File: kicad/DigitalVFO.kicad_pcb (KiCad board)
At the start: 2 copper layers, 99.6 x 49.8 mm, 34 parts, among them Q1 2N2222A, U1 74HC14, U2 Teensy3.2, U3 LCD1602A, U4 DDS-60

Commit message: Version 1.4
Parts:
- removed Battery: Battery, DigitalVFO:Conn_Power_2
- removed RF out: RF Out, DigitalVFO:BNC_Socket
- removed Rotary Encoder: Rotary_Encoder_Switch, DigitalVFO:Conn_RE_Switch
- removed SW_LED: SW_LED, DigitalVFO:Conn_Power_2
- added C8: 0.1uF, DigitalVFO:Cap_SmV, F.Cu at (182.9, 115.6)
- added J1: RF Out, DigitalVFO:BNC_Socket_TYCO-AMP, F.Cu at (214.6, 113.3)
- added J2: Battery, DigitalVFO:Conn_Power_2, F.Cu at (149.1, 112.3)
- added J3: SW_LED, DigitalVFO:Conn_Power_2, F.Cu at (174.8, 112.3)
- added R12: 39K, DigitalVFO:Res_SmH, F.Cu at (185.4, 109.7)
- added R13: 10K, DigitalVFO:Res_SmH, F.Cu at (185.4, 112.8)
- added SW1: Rotary_Encoder, DigitalVFO:Conn_RE_Switch, F.Cu at (161.8, 112.3)
- moved REF** 11.0 mm to (198.9, 112.5)
- moved R9 3.30 mm to (183.9, 102.4)
- moved R10 3.21 mm to (180.8, 102.6)
- moved C4 2.50 mm to (187.5, 102.4)
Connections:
- U2 pad 21: (no net) -> Net-(C8-Pad1)
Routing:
- net Net-(C8-Pad1): track 0.00 -> 32.3 mm
- net Net-(D1-Pad2): track 7.95 -> 38.4 mm
- net Net-(J1-Pad1): track 90.8 -> 86.3 mm
- net Net-(R9-Pad2): track 34.5 -> 30.7 mm
- net Net-(C4-Pad1): track 46.6 -> 44.1 mm
- net Net-(C2-Pad1): track 14.0 -> 14.7 mm
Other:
- net class Default: trace_width 0.25 -> 0.5
- board text added: "DigitalVFO 1.4 27 Apr 2018 vk4fawr"
- board text removed: "DigitalVFO 1.2 26 Mar 2018 vk4fawr"

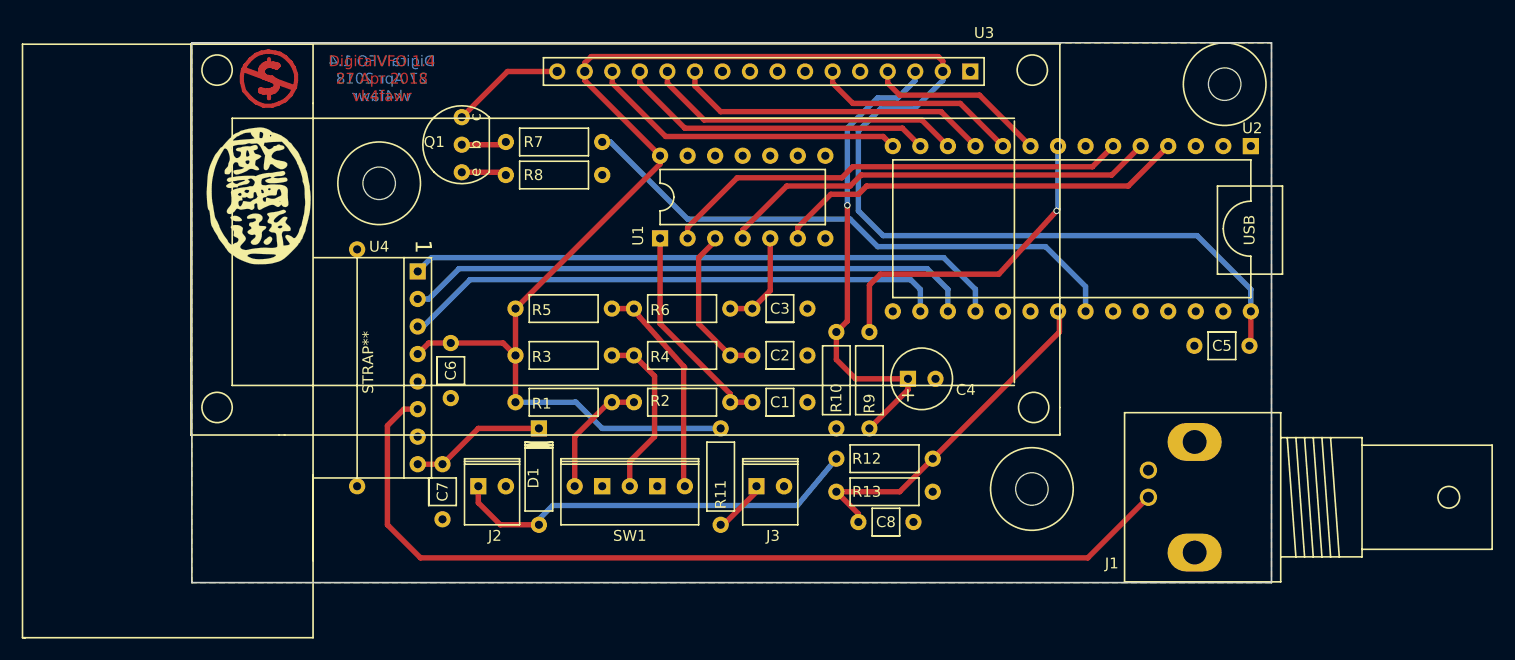
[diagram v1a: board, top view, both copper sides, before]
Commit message: v1.5 - more compact layout
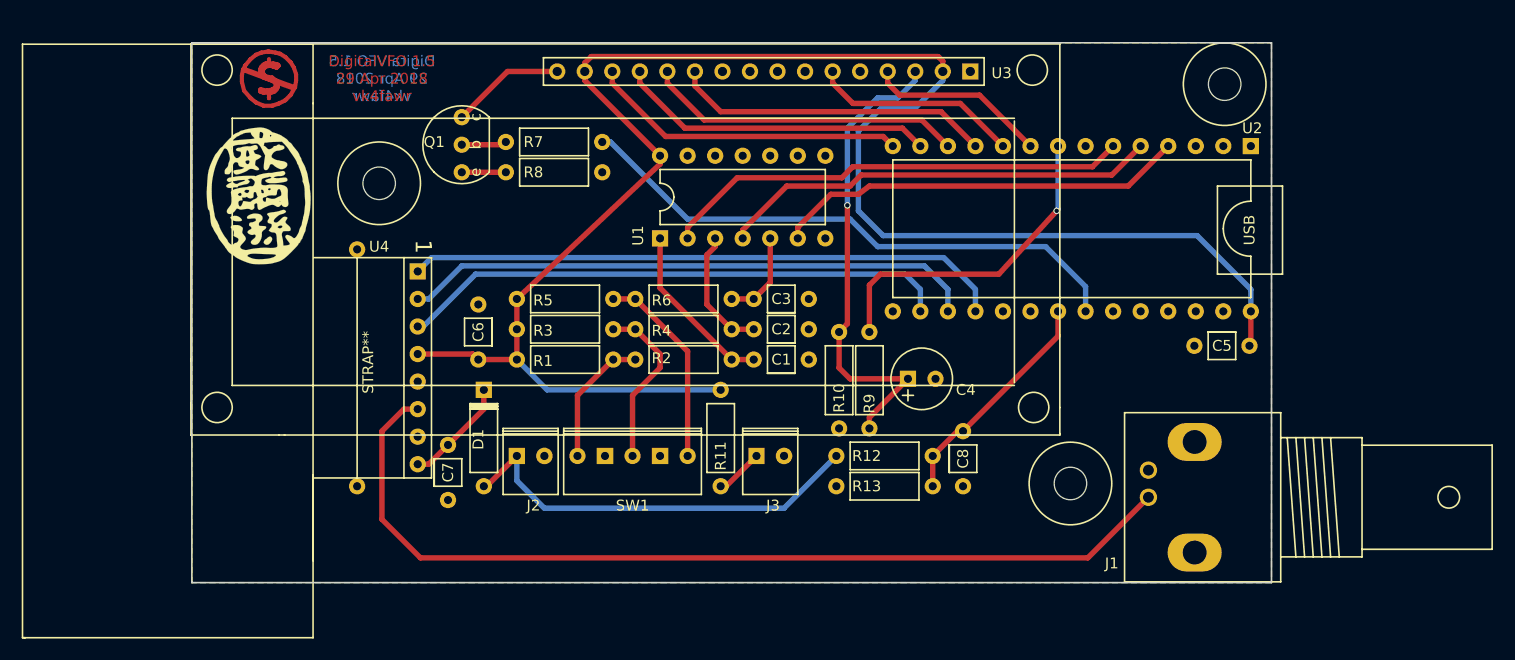
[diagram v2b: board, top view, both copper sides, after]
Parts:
- R12: value 39K -> 22K
- moved C8 12.8 mm to (192.5, 107.2), turned to 270 degrees
- moved D1 6.20 mm to (148.3, 108.0)
- moved J2 4.52 mm to (152.7, 109.5)
- moved C1 3.94 mm to (173.2, 100.6)
- moved R1 3.94 mm to (156.0, 100.6)
- moved R2 3.94 mm to (166.9, 100.6)
- moved REF** 3.59 mm to (202.4, 112.0)
- moved R11 3.56 mm to (170.2, 108.0)
- moved C6 2.96 mm to (147.8, 100.6), turned to 90 degrees
- moved SW1 2.81 mm to (162.1, 109.5)
- moved J3 2.79 mm to (174.8, 109.5)
- moved C2 2.42 mm to (173.2, 97.8)
- moved R3 2.42 mm to (156.0, 97.8)
- moved R4 2.42 mm to (166.9, 97.8)
- moved C7 1.85 mm to (145.0, 108.5)
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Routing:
- net Net-(C8-Pad1): track 32.3 -> 21.6 mm
- net +5V: track 166.3 -> 162.3 mm
- net Net-(C1-Pad1): track 19.8 -> 15.9 mm
- net Net-(C2-Pad1): track 14.7 -> 11.9 mm
- net Net-(C7-Pad1): track 12.5 -> 9.98 mm
- net Net-(R5-Pad2): track 20.8 -> 18.8 mm
- net Net-(D1-Pad2): track 38.4 -> 39.5 mm
- net Net-(C3-Pad1): track 9.19 -> 8.25 mm
- net Net-(R1-Pad2): track 11.6 -> 12.5 mm
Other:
- board text added: "DigitalVFO 1.5 29 Apr 2018 vk4fawr"
- board text removed: "DigitalVFO 1.4 27 Apr 2018 vk4fawr"

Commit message: Added testpoints and 1602A mount holes
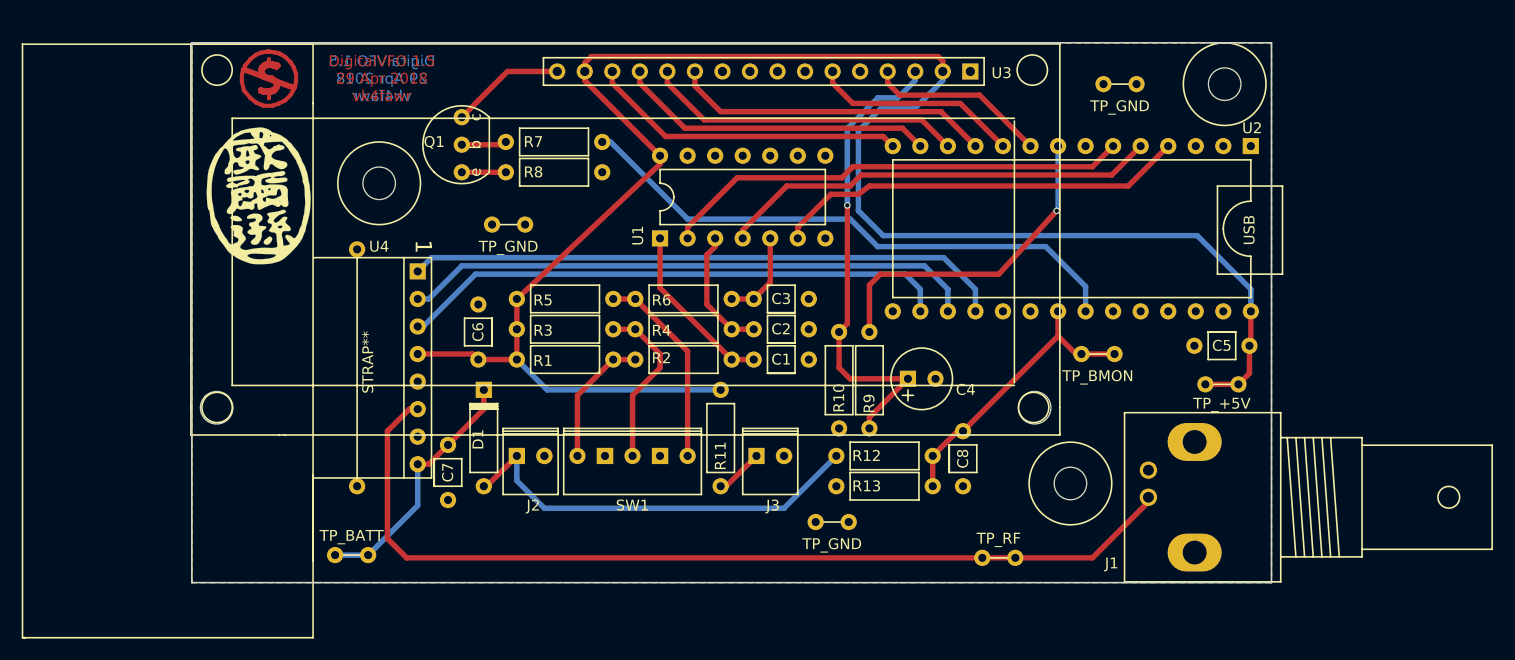
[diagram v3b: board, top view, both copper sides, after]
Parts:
- added REF**: MountHole_M3, DigitalVFO:MountHole_M3, F.Cu at (199.1, 105.0)
- added REF**: MountHole_M3, DigitalVFO:MountHole_M3, F.Cu at (123.7, 105.0)
- added TP_+5V: TestPoint, DigitalVFO:TestPoint, F.Cu at (216.4, 102.9)
- added TP_BATT: TestPoint, DigitalVFO:TestPoint, F.Cu at (136.1, 118.6)
- added TP_BMON: TestPoint, DigitalVFO:TestPoint, F.Cu at (205.0, 100.1)
- added TP_GND: TestPoint, DigitalVFO:TestPoint, F.Cu at (207.0, 75.2)
- added TP_GND: TestPoint, DigitalVFO:TestPoint, F.Cu at (150.6, 88.1)
- added TP_GND: TestPoint, DigitalVFO:TestPoint, F.Cu at (180.5, 115.6)
- added TP_RF: TestPoint, DigitalVFO:TestPoint, F.Cu at (195.8, 118.9)
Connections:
- net Net-(C7-Pad1) renamed /BATT
- net Net-(C8-Pad1) renamed /BMON
- net Net-(J1-Pad1) renamed /RF
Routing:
- net /BATT: track 9.98 -> 23.3 mm
- net +5V: track 162.3 -> 169.3 mm
- net /BMON: track 21.6 -> 27.5 mm

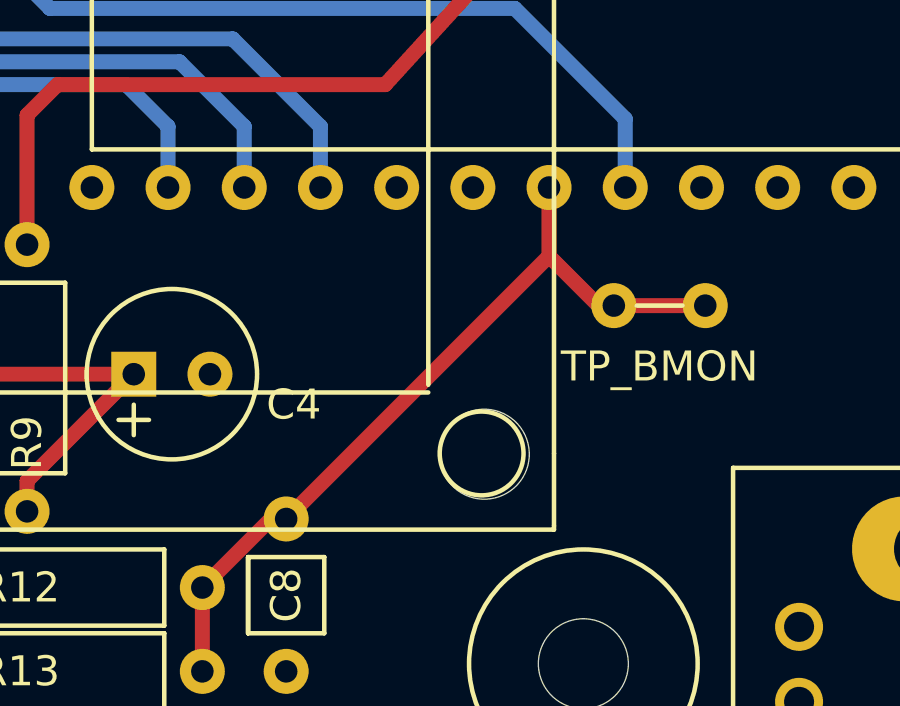
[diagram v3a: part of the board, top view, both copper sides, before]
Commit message: Moved track away from LCD mount hole
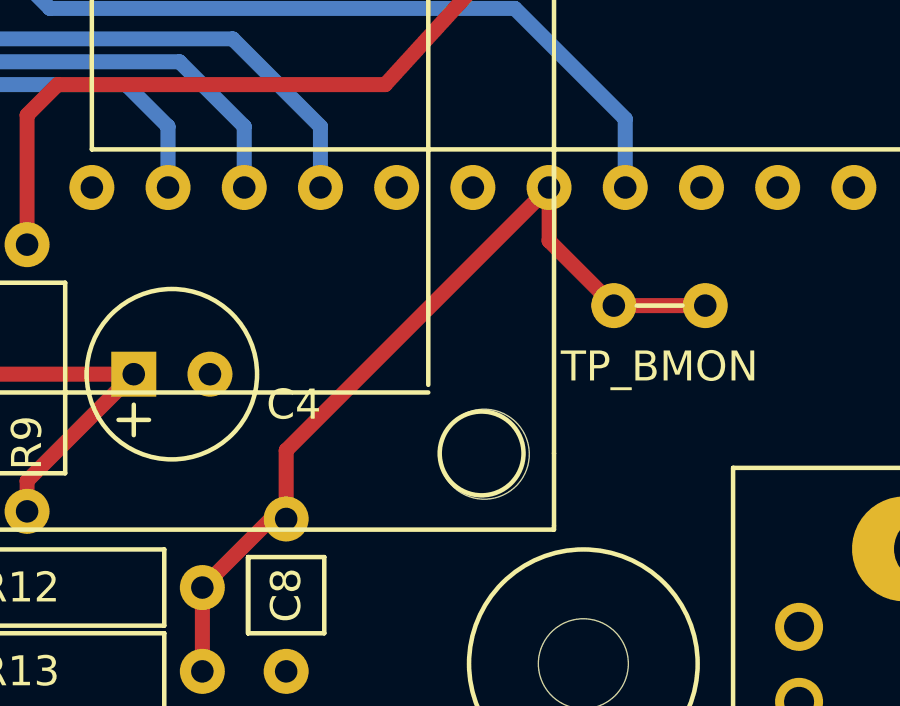
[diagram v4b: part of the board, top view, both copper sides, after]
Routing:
- net /BMON: track 27.5 -> 30.3 mm
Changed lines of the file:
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@@
     (thickness 1.6)
     (drawings 7)
-    (tracks 184)
+    (tracks 186)
     (zones 0)
     (modules 46)
@@
   (segment (start 190.754 91.186) (end 143.51 91.186) (width 0.5) (layer B.Cu) (net 31))
   (segment (start 193.675 94.107) (end 190.754 91.186) (width 0.5) (layer B.Cu) (net 31))
+  (segment (start 201.295 96.139) (end 201.295 97.917) (width 0.5) (layer F.Cu) (net 33))
+  (segment (start 201.295 97.917) (end 203.454 100.076) (width 0.5) (layer F.Cu) (net 33))
+  (segment (start 201.295 96.139) (end 201.549 96.139) (width 0.5) (layer F.Cu) (net 33))
+  (segment (start 192.532 107.188) (end 192.532 104.902) (width 0.5) (layer F.Cu) (net 33))
+  (segment (start 192.532 104.902) (end 201.295 96.139) (width 0.5) (layer F.Cu) (net 33))
   (segment (start 203.454 100.076) (end 206.502 100.076) (width 0.5) (layer F.Cu) (net 33))
-  (segment (start 201.295 98.425) (end 202.946 100.076) (width 0.5) (layer F.Cu) (net 33))
   (segment (start 202.946 100.076) (end 203.454 100.076) (width 0.5) (layer F.Cu) (net 33))
-  (segment (start 201.295 96.139) (end 201.295 98.425) (width 0.5) (layer F.Cu) (net 33))
   (segment (start 189.738 109.474) (end 189.738 112.268) (width 0.5) (layer F.Cu) (net 33))
   (segment (start 192.532 107.188) (end 192.024 107.188) (width 0.5) (layer F.Cu) (net 33))
   (segment (start 192.024 107.188) (end 189.738 109.474) (width 0.5) (layer F.Cu) (net 33))
-  (segment (start 201.295 98.425) (end 192.532 107.188) (width 0.5) (layer F.Cu) (net 33))
   (segment (start 192.786 107.188) (end 192.532 107.188) (width 0.5) (layer F.Cu) (net 33) (status 30))
   (segment (start 201.422 96.266) (end 201.295 96.139) (width 0.5) (layer F.Cu) (net 33))
